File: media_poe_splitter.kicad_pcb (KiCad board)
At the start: 4 copper layers, 70.7 x 66.1 mm, 76 parts, among them IC1 LAN7850-I_8JX, IC2 17791063215, IC3 93AA66C-I/SN, J1 Screw_Terminal_01x02, X1 7499811120, X2 68710614522, Y1 830055299

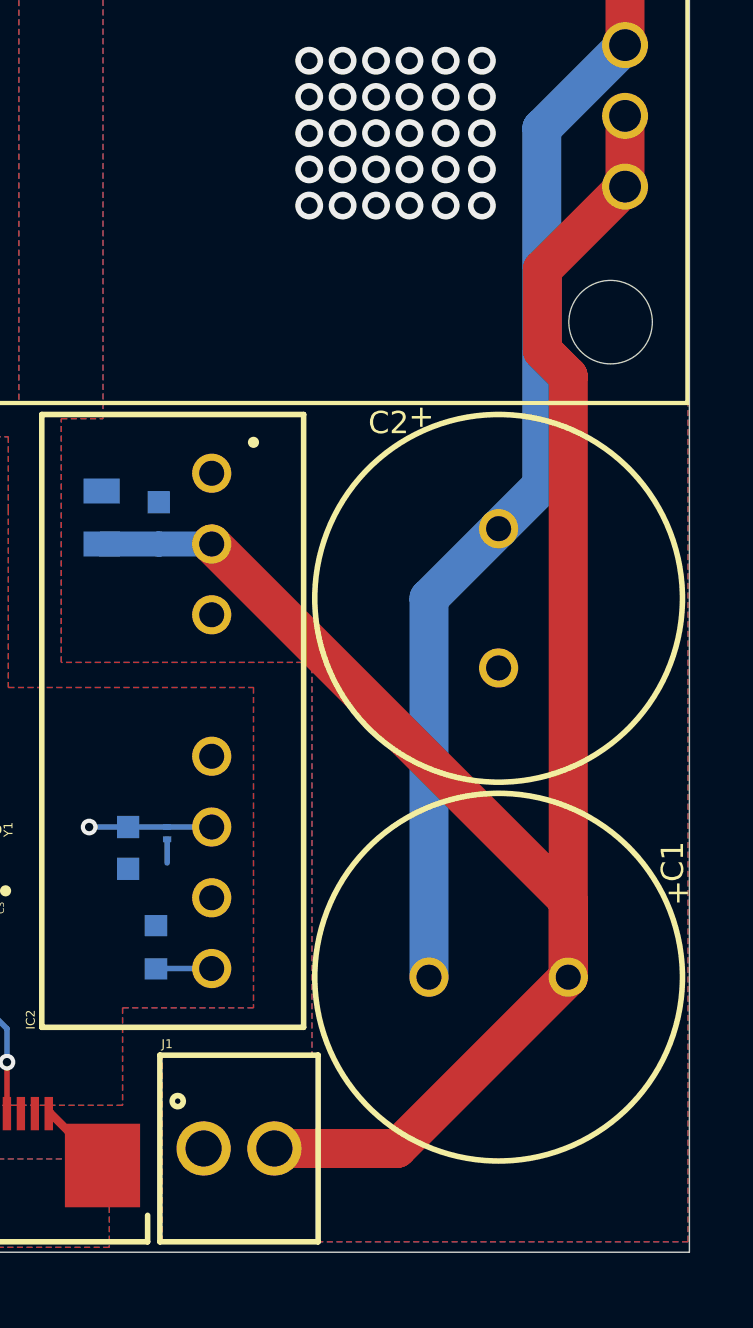
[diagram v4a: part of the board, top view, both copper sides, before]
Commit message: poe splitter: transform output to be in series to allow switching it off
Signed-off-by: Marc 'risson' Schmitt <marc.schmitt@risson.space>
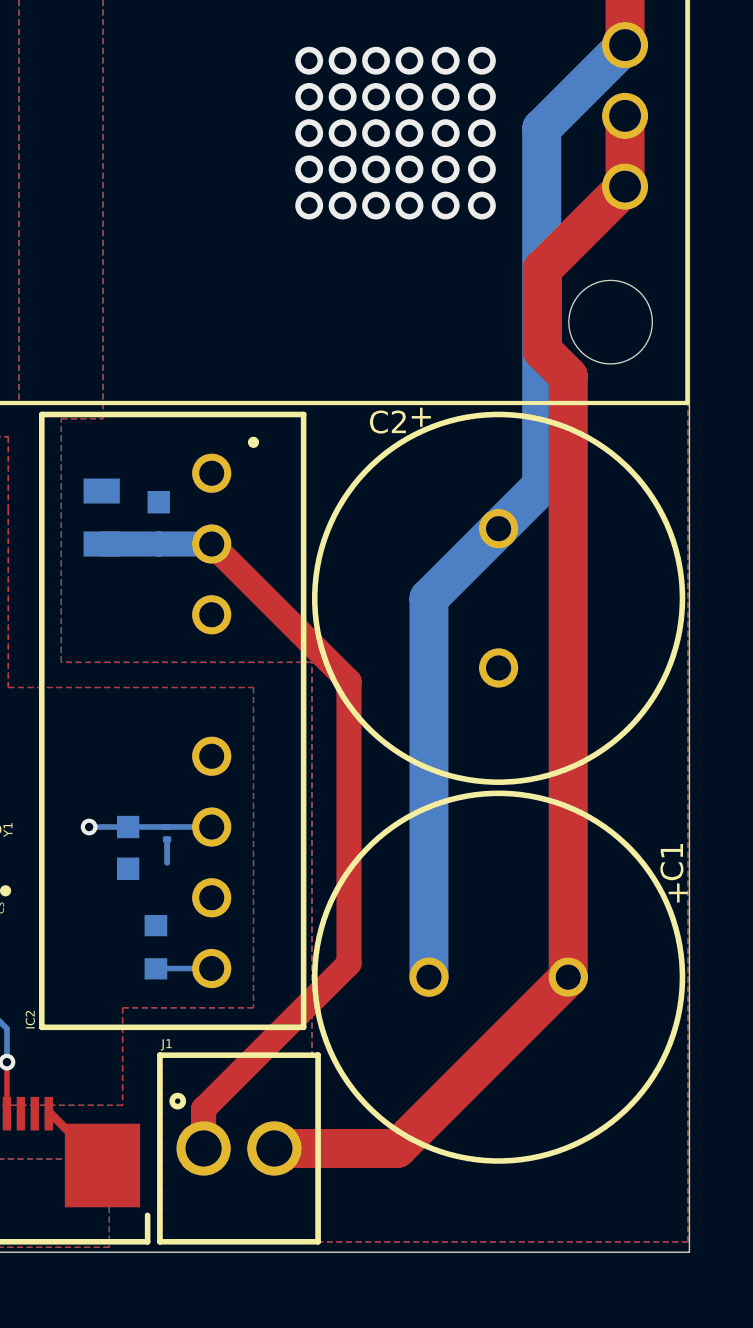
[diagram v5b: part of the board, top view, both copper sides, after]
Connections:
- B1 pad 10: +24V -> Net-(B1-VOUT2-Pad10)
- B1 pad 9: +24V -> Net-(B1-VOUT2-Pad10)
- C1 pad 1: +24V -> Net-(B1-VOUT2-Pad10)
- C4 pad 1: +24V -> Net-(IC2-+VIN)
- C7 pad 1: +24V -> Net-(IC2-+VIN)
- IC2 pad 2: +24V -> Net-(IC2-+VIN)
- J1 pad 1: GNDA -> Net-(IC2-+VIN)
- J1 pad 2: +24V -> Net-(B1-VOUT2-Pad10)
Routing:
- net +24V: track 70.4 -> 0.00 mm
- net Net-(B1-VOUT2-Pad10): track 0.00 -> 45.6 mm
- net Net-(IC2-+VIN): track 0.00 -> 29.9 mm
